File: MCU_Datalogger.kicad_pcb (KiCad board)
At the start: 2 copper layers, 50 x 30 mm, 29 parts, among them J1 Conn_01x04_Pin, J2 Conn_01x04_Pin, J3 Conn_01x09_Pin, J4 Conn_02x03_Odd_Even, U1 24LC1025, U2 DS1337S_, U3 24LC1025, U4 ATMEGA328P-AU, Y1 32.768 KHz, Y2 16 MHz

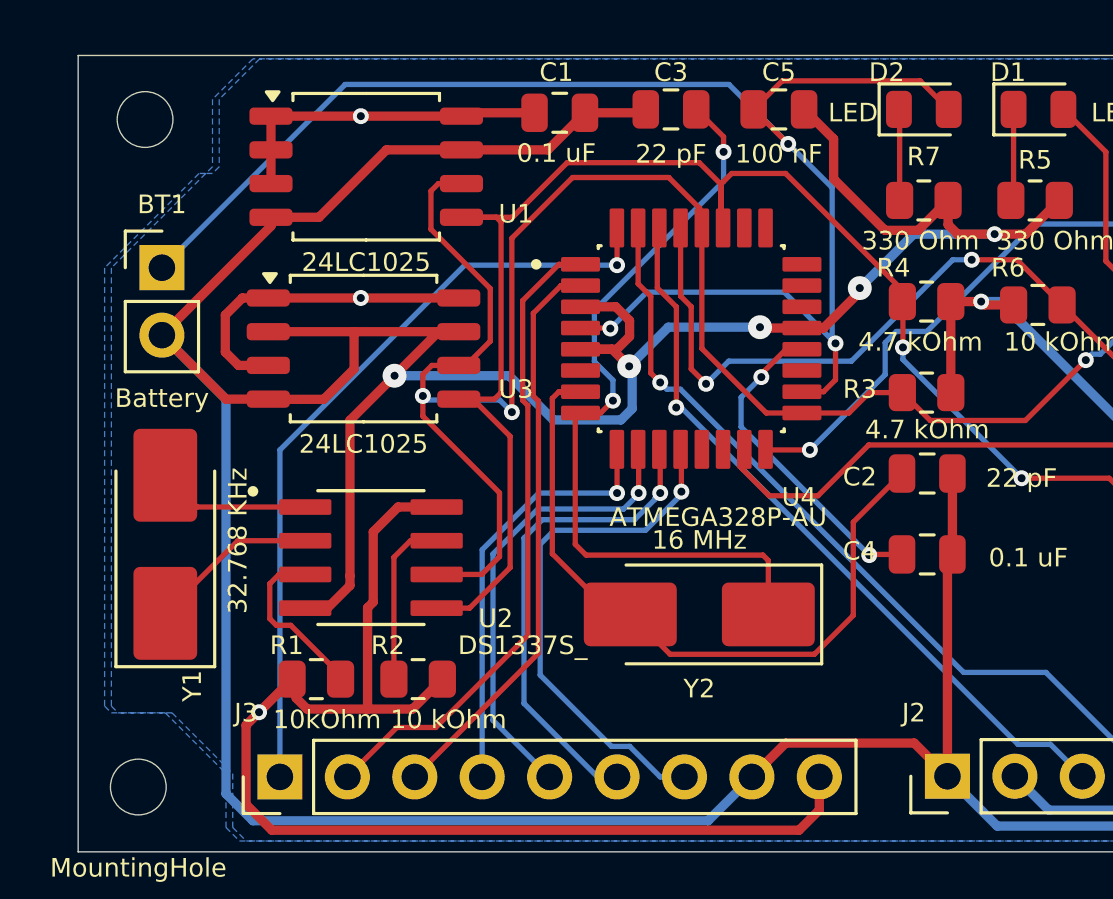
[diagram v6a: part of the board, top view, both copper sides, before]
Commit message: fixed issue with VCC
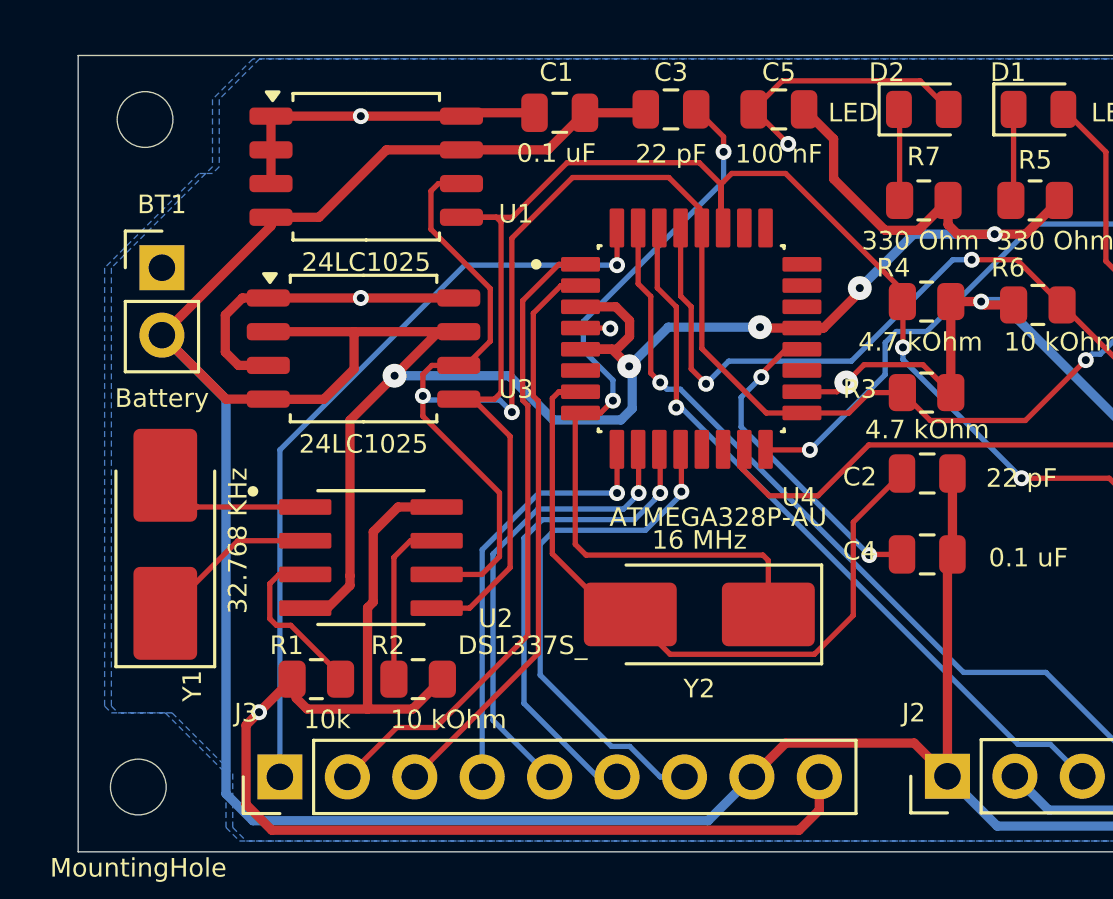
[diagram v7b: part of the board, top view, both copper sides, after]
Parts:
- R1: value 10kOhm -> 10k
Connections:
- BT1 pad 1: Net-(BT1-+) -> /Vcc
- C5 pad 1: Net-(BT1-+) -> /Vcc
- D2 pad 2: Net-(BT1-+) -> /Vcc
- U4 pad 18: Net-(BT1-+) -> /Vcc
- U4 pad 4: Net-(BT1-+) -> /Vcc
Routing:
- net Net-(BT1-+): track 59.6 -> 0.00 mm, vias 3 -> 0
- net /Vcc: track 108.3 -> 126.3 mm, vias 4 -> 7

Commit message: added manufacturing information
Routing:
- net /D8: track 19.8 -> 21.2 mm
- net /D7: track 18.4 -> 19.0 mm
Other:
- board text added: "0"
- board text added: "0 mm"
- board text added: "0.0000 mm / 0.0000 mm"
- board text added: "0.01 mm"
- board text added: "0.02"
- board text added: "0.035 mm"
- board text added: "0.3000 mm"
- board text added: "1"
- board text added: "1.51 mm"
- board text added: "1.6000 mm"
- board text added: "2"
- board text added: "3.3"
- board text added: "4.5"
- board text added: "50.0000 mm x 30.0000 mm"
- board text added: "B.Cu"
- board text added: "B.Mask"
- board text added: "B.Paste"
- board text added: "B.Silkscreen"
- board text added: "BOARD CHARACTERISTICS"
- board text added: "Board Thickness:"
- board text added: "Board overall dimensions:"
- board text added: "Bottom Silk Screen"
- board text added: "Bottom Solder Mask"
- board text added: "Bottom Solder Paste"
- board text added: "Castellated pads:"
- board text added: "Color"
- board text added: "Copper Finish:"
- board text added: "Copper Layer Count:"
- board text added: "Dielectric"
- board text added: "Edge card connectors:"
- board text added: "Epsilon R"
- board text added: "F.Cu"
- board text added: "F.Mask"
- board text added: "F.Paste"
- board text added: "F.Silkscreen"
- board text added: "FR4"
- board text added: "Impedance Control:"
- board text added: "Layer Name"
- board text added: "Loss Tangent"
- board text added: "Material"
- board text added: "Min hole diameter:"
- board text added: "Min track/spacing:"
- board text added: "No"
- board text added: "None"
- board text added: "Not specified"
- board text added: "Plated Board Edge:"
- board text added: "Thickness (mm)"
- board text added: "Top Silk Screen"
- board text added: "Top Solder Mask"
- board text added: "Top Solder Paste"
- board text added: "Type"
- board text added: "copper"
- board text added: "core"
